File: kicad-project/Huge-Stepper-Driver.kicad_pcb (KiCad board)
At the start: 2 copper layers, 99.1 x 61 mm, 103 parts, among them J1 Screw_Terminal_01x02, J13 Conn_01x04_Male, J14 Conn_01x04_Male, J2 USB_C_Receptacle_USB2.0, J21 Motor 1, J3 Conn_02x04_Odd_Even, J4 Conn_01x02_Female, J5 Conn_01x02_Female, J6 Conn_01x02_Female, J7 Conn_01x04_Male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

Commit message: fix unipolar e qualche rotta
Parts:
- moved R34 1.45 mm to (110.1, 123.6)
- moved R35 1.45 mm to (110.1, 127.4)
- moved R36 1.45 mm to (110.1, 131.1)
- moved R37 1.45 mm to (110.1, 134.9)
- moved R38 1.45 mm to (110.1, 121.8)
- moved R39 1.45 mm to (110.1, 125.5)
- moved R40 1.45 mm to (110.1, 129.3)
- moved R41 1.45 mm to (110.1, 133.0)
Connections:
- D10 pad 1: +12V -> +5V
- D8 pad 1: +12V -> +5V
- D9 pad 1: +12V -> +5V
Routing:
- net GND: track 0.00 -> 27.2 mm, vias 0 -> 6
- net +5V: track 0.00 -> 18.6 mm
- net /Unipolar Driver /M1_OUT1: track 0.00 -> 13.8 mm, vias 0 -> 2
- net /Unipolar Driver /M1_OUT2: track 0.00 -> 12.6 mm, vias 0 -> 2
- net /Unipolar Driver /M1_OUT3: track 0.00 -> 12.3 mm, vias 0 -> 2
- net /Unipolar Driver /M1_OUT4: track 0.00 -> 11.8 mm
- net Net-(Q5-Pad1): track 0.00 -> 6.63 mm
- net Net-(Q8-Pad1): track 0.00 -> 6.60 mm
- net Net-(Q6-Pad1): track 0.00 -> 6.59 mm
- net Net-(Q7-Pad1): track 0.00 -> 6.56 mm

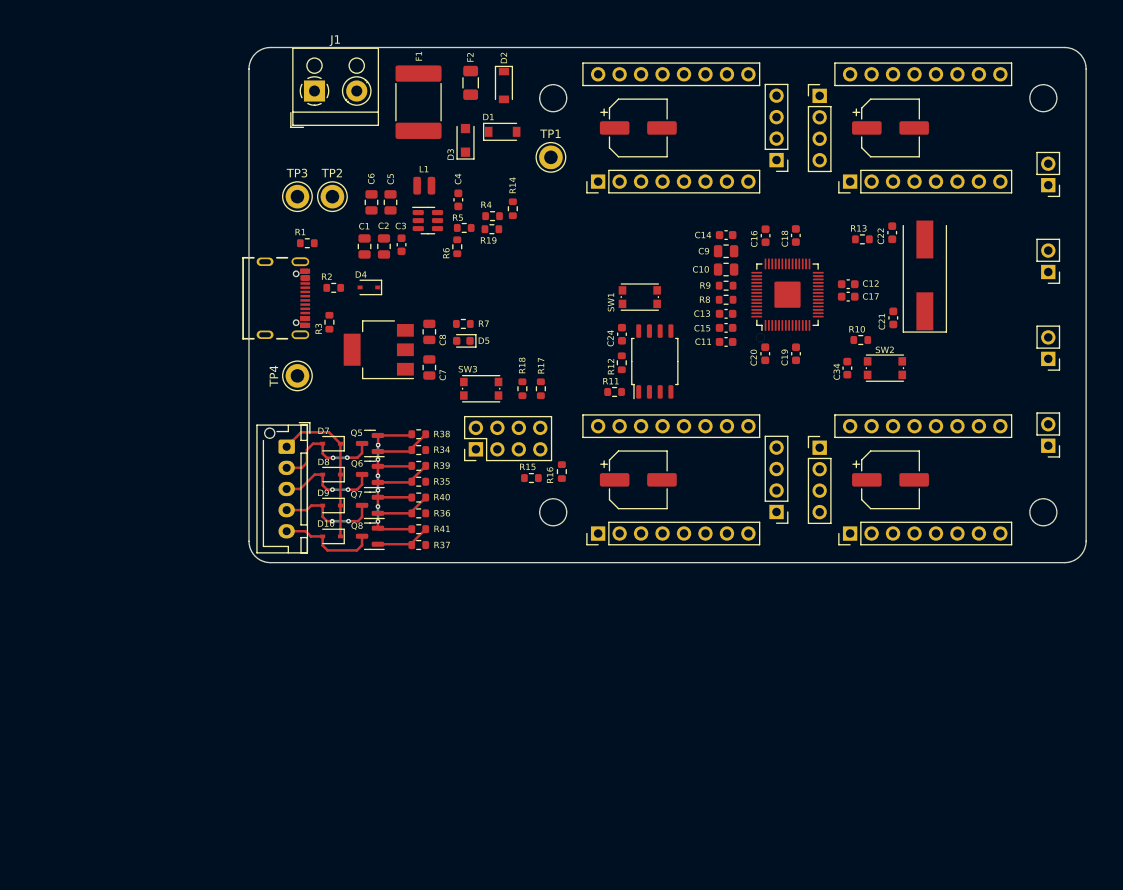
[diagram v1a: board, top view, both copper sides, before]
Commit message: hw: HSD v1.0 w/out peripherals
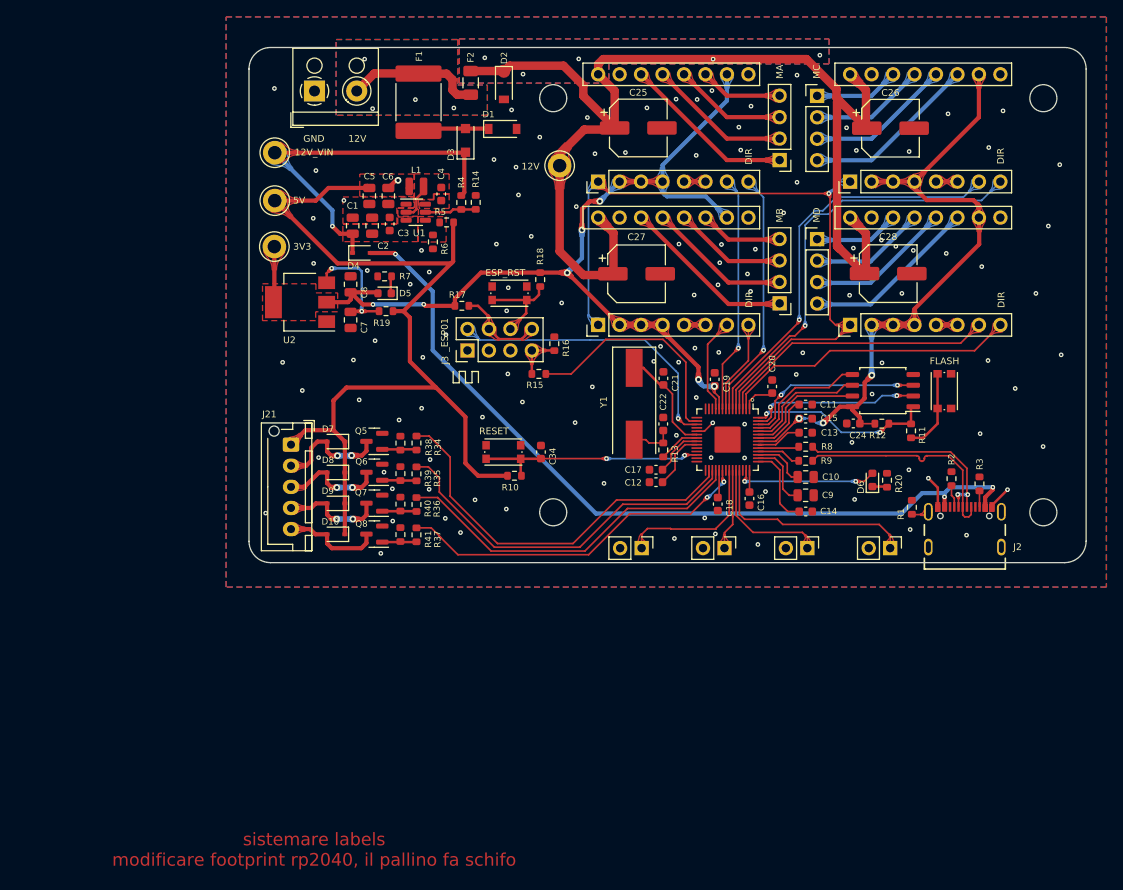
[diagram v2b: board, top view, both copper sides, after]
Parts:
- added D6: PWR_LED, LED_SMD:LED_0603_1608Metric, F.Cu at (163.8, 127.2)
- added R20: 510, Resistor_SMD:R_0603_1608Metric, F.Cu at (165.5, 127.2)
- moved J2 87.9 mm to (174.7, 135.1), turned to 0 degrees
- moved R3 79.3 mm to (176.4, 127.6), turned to 90 degrees
- moved R1 78.1 mm to (168.4, 130.4), turned to 90 degrees
- moved R2 76.5 mm to (173.1, 127.0), turned to 90 degrees
- moved J4 64.5 mm to (136.5, 135.2), turned to -90 degrees
- moved J5 50.4 mm to (146.3, 135.2), turned to -90 degrees
- moved SW2 46.2 mm to (120.1, 123.9), turned to 180 degrees
- moved R10 44.0 mm to (121.4, 126.7)
- moved SW1 37.7 mm to (172.3, 116.7), turned to 90 degrees
- moved Y1 37.6 mm to (135.6, 118.2), turned to -90 degrees
- moved C34 37.6 mm to (124.5, 123.9), turned to 90 degrees
- moved J6 36.3 mm to (156.1, 135.2), turned to -90 degrees
- moved R11 35.4 mm to (168.3, 121.4), turned to 90 degrees
- moved C22 35.3 mm to (139.0, 120.5)
- moved R13 34.3 mm to (139.0, 123.6), turned to -90 degrees
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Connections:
- J3 pad 2: /MCU/ESP_TX -> /MCU/MCU_UART0_RX
- R15 pad 1: /MCU/ESP_RX -> /MCU/MCU_UART0_TX
- R6 pad 1: unconnected-(R6-Pad1) -> GND
- R6 pad 2: unconnected-(R6-Pad2) -> /Power Management/SW_FB
- U3 pad 11: /MCU/STEP_A -> /MCU/STEP_B
- U3 pad 12: /MCU/DIR_A -> unconnected-(U3-Pad12)
- U3 pad 13: /MCU/STEP_B -> unconnected-(U3-Pad13)
- U3 pad 14: /MCU/DIR_B -> unconnected-(U3-Pad14)
- U3 pad 15: /MCU/STEP_C -> unconnected-(U3-Pad15)
- U3 pad 16: /MCU/DIR_C -> /MCU/MCU_UART0_TX
- U3 pad 17: /MCU/STEP_D -> /MCU/MCU_UART0_RX
- U3 pad 18: /MCU/DIR_D -> unconnected-(U3-Pad18)
- U3 pad 2: /MCU/ESP_RX -> /MCU/DIR_D
- U3 pad 27: /MCU/ME_W11 -> unconnected-(U3-Pad27)
- U3 pad 28: /MCU/ME_W12 -> unconnected-(U3-Pad28)
- U3 pad 29: /MCU/ME_W21 -> unconnected-(U3-Pad29)
- U3 pad 3: /MCU/ESP_TX -> /MCU/STEP_D
- U3 pad 30: /MCU/ME_W22 -> /MCU/ME_W11
- U3 pad 31: /Bipolar Drivers/LS1 -> /MCU/ME_W12
- U3 pad 32: /Bipolar Drivers/LS2 -> /MCU/ME_W21
- U3 pad 34: /Bipolar Drivers/LS3 -> /MCU/ME_W22
- U3 pad 35: /Bipolar Drivers/LS4 -> unconnected-(U3-Pad35)
- U3 pad 36: unconnected-(U3-Pad36) -> /Bipolar Drivers/LS1
- U3 pad 37: unconnected-(U3-Pad37) -> /Bipolar Drivers/LS2
- U3 pad 38: unconnected-(U3-Pad38) -> /Bipolar Drivers/LS3
- U3 pad 39: unconnected-(U3-Pad39) -> /Bipolar Drivers/LS4
- U3 pad 4: unconnected-(U3-Pad4) -> /MCU/EN_MOTOR
- U3 pad 41: unconnected-(U3-Pad41) -> Net-(D6-Pad2)
- U3 pad 5: unconnected-(U3-Pad5) -> /MCU/DIR_C
- U3 pad 6: unconnected-(U3-Pad6) -> /MCU/STEP_C
- U3 pad 7: unconnected-(U3-Pad7) -> /MCU/DIR_A
- U3 pad 8: unconnected-(U3-Pad8) -> /MCU/DIR_B
- U3 pad 9: /MCU/EN_MOTOR -> /MCU/STEP_A
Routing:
- net +3V3: track 0.00 -> 236.2 mm, vias 0 -> 10
- net +12V: track 0.00 -> 137.4 mm, vias 0 -> 5
- net /Power Management/VBUS: track 0.00 -> 96.2 mm, vias 0 -> 3
- net +5V: track 18.6 -> 113.9 mm, vias 0 -> 1
- net /MCU/EN_MOTOR: track 0.00 -> 85.0 mm, vias 0 -> 1
- net /MCU/DIR_C: track 0.00 -> 50.7 mm, vias 0 -> 1
- net /MCU/STEP_C: track 0.00 -> 48.3 mm, vias 0 -> 1
- net /MCU/ME_W11: track 0.00 -> 46.6 mm
- net /Power Management/SW_VIN: track 0.00 -> 45.1 mm, vias 0 -> 1
- net /MCU/ME_W12: track 0.00 -> 44.3 mm
- net /MCU/ME_W22: track 0.00 -> 43.0 mm, vias 0 -> 2
- net /MCU/ME_W21: track 0.00 -> 42.7 mm
- net /MCU/DIR_D: track 0.00 -> 35.2 mm
- net /MCU/MCU_UART0_RX: track 0.00 -> 34.9 mm, vias 0 -> 1
- net /MCU/STEP_D: track 0.00 -> 33.2 mm
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- added copper zone on B.Cu, net +12V
- added copper zone on F.Cu, net +12V
- added copper zone on F.Cu, net +3V3
- added copper zone on F.Cu, net +5V
- added copper zone on B.Cu, net /Power Management/12V_IN
- added copper zone on F.Cu, net /Power Management/12V_IN
- added copper zone on F.Cu, net /Power Management/SW_BST
- added copper zone on F.Cu, net /Power Management/SW_FB
- added copper zone on F.Cu, net /Power Management/SW_NODE
- added copper zone on F.Cu, net /Power Management/SW_VIN
- added copper zone on B.Cu, net GND
- added copper zone on F.Cu, net GND
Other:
- board text added: "-"
- board text added: "12V"
- board text added: "12V_VIN"
- board text added: "3V3"
- board text added: "5V"
- board text added: "DIR"
- board text added: "ESP_RST"
- board text added: "FLASH"
- board text added: "GND"
- board text added: "LA"
- board text added: "LB"
- board text added: "LC"
- board text added: "LD"
- board text added: "MA"
- board text added: "MB"
- board text added: "MC"
- board text added: "MD"
- board text added: "RESET"
- board text added: "VIN"
- board text added: "_ESP01"
- board text added: "sistemare labels modificare footprint rp2040, il pallino fa schifo"

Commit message: hw: updated HSD v1.0 + add gerber files
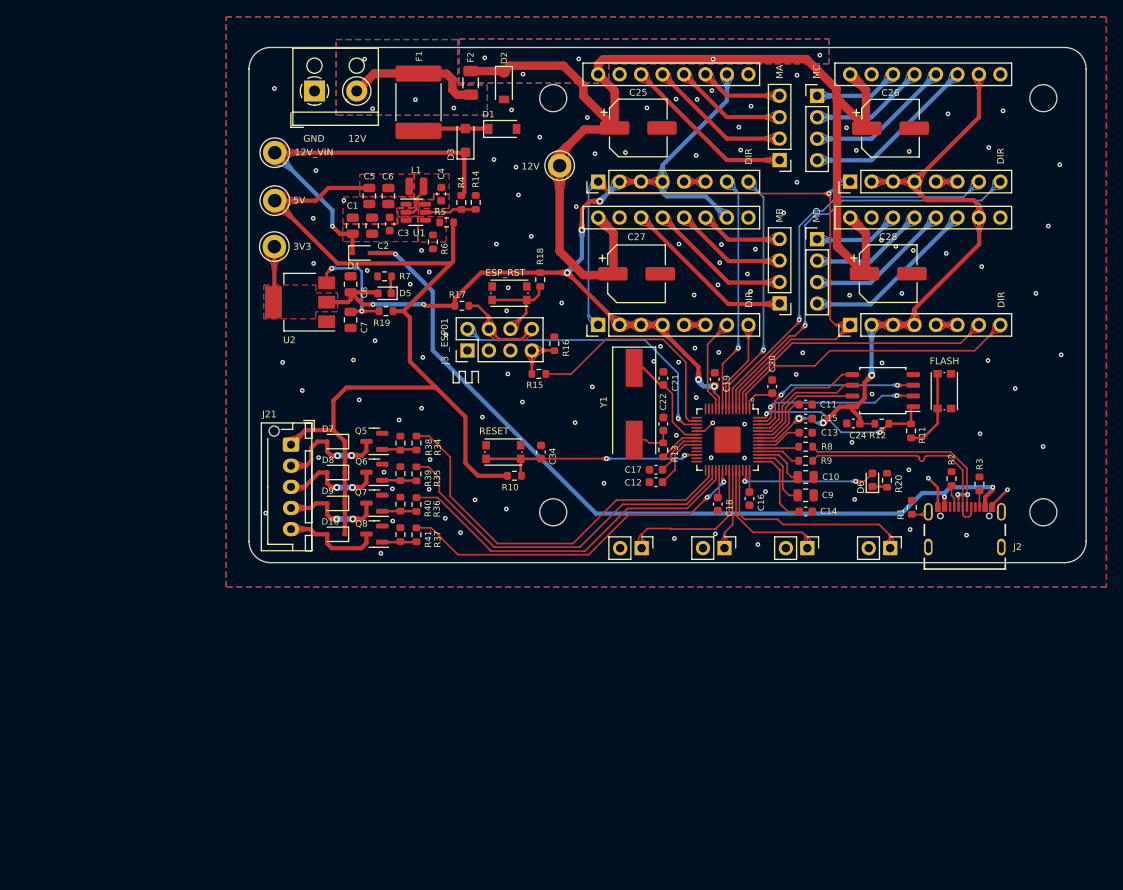
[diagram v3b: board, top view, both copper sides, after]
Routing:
- net +5V: track 113.9 -> 112.4 mm, vias 1 -> 0
- net GND: vias 117 -> 116
- net (no net): vias 1 -> 0
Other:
- board text removed: "100x60mm"
- board text removed: "sistemare labels modificare footprint rp2040, il pallino fa schifo"
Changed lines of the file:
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@@
       (outputformat 1)
       (mirror false)
-      (drillshape 1)
+      (drillshape 0)
       (scaleselection 1)
-      (outputdirectory "")
+      (outputdirectory "/Users/macbookpro/Desktop/HSD-RP2040-5-stepper-motor-driver/kicad-project/gerber")
     )
   )
@@
     (fp_line (start 3.6775 2.56) (end -3.6775 2.56) (layer "F.Fab") (width 0.1))
     (fp_line (start -3.6775 2.56) (end -3.6775 -2.56) (layer "F.Fab") (width 0.1))
-    (pad "1" smd roundrect (at -3.3875 0 90) (size 1.925 5.45) (layers "F.Cu" "F.Paste" "F.Mask") (roundrect_rratio 0.12987)
+    (pad "1" smd roundrect (at -3.3875 0 90) (size 1.925 5.45) (layers "F.Cu" "F.Paste" "F.Mask") (roundrect_rratio 0.1298701299)
       (net 12 "/Power Management/12V_Post_PPTC") (pintype "passive"))
-    (pad "2" smd roundrect (at 3.3875 0 90) (size 1.925 5.45) (layers "F.Cu" "F.Paste" "F.Mask") (roundrect_rratio 0.12987)
+    (pad "2" smd roundrect (at 3.3875 0 90) (size 1.925 5.45) (layers "F.Cu" "F.Paste" "F.Mask") (roundrect_rratio 0.1298701299)
       (net 19 "/Power Management/12V_IN") (pintype "passive"))
     (model "${KICAD6_3DMODEL_DIR}/Fuse.3dshapes/Fuse_2920_7451Metric.wrl"
@@
     (fp_line (start 0 -1.35) (end 0.625 -2.35) (layer "F.Fab") (width 0.1))
     (pad "" np_thru_hole circle (at -1.6 2 270) (size 1.2 1.2) (drill 1.2) (layers *.Cu *.Mask))
-    (pad "1" thru_hole roundrect (at 0 0 270) (size 1.7 1.95) (drill 0.95) (layers *.Cu *.Mask) (roundrect_rratio 0.147059)
+    (pad "1" thru_hole roundrect (at 0 0 270) (size 1.7 1.95) (drill 0.95) (layers *.Cu *.Mask) (roundrect_rratio 0.1470588235)
       (net 5 "+5V") (pinfunction "Pin_1") (pintype "passive"))
     (pad "2" thru_hole oval (at 2.5 0 270) (size 1.7 1.95) (drill 0.95) (layers *.Cu *.Mask)
@@
   (gr_circle (center 126 131) (end 129 131) (layer "Margin") (width 0.15) (fill none))
   (gr_circle (center 184 131) (end 187 131) (layer "Margin") (width 0.15) (fill none))
-  (gr_text "sistemare labels\nmodificare footprint rp2040, il pallino fa schifo" (at 97.71 170.92) (layer "F.Cu")
-    (effects (font (size 1.5 1.5) (thickness 0.3)))
-  )
   (gr_text "3V3" (at 96.35 99.56) (layer "B.SilkS")
     (effects (font (size 0.8 0.8) (thickness 0.15)) (justify mirror))
@@
     (effects (font (size 0.8 0.8) (thickness 0.15)))
   )
-  (gr_text "100x60mm\n" (at 93.525 74.4) (layer "Edge.Cuts")
-    (effects (font (size 1 1) (thickness 0.15)))
-  )
   (gr_text "58x49mm\n" (at 242.75 54.1) (layer "F.Fab")
     (effects (font (size 1 1) (thickness 0.15)))
   )
-  (via (at 161.52 99.74) (size 0.55) (drill 0.25) (layers "F.Cu" "B.Cu") (free) (net 0))
   (segment (start 102.13 98.1814) (end 102.2712 98.0402) (width 0.5) (layer "F.Cu") (net 1))
   (segment (start 93.05 88.45) (end 115.5658 88.45) (width 0.5) (layer "F.Cu") (net 1))
@@
   (via (at 148.64 124.57) (size 0.55) (drill 0.25) (layers "F.Cu" "B.Cu") (free) (net 2))
   (via (at 142.93 117.42) (size 0.55) (drill 0.25) (layers "F.Cu" "B.Cu") (free) (net 2))
-  (via (at 143.93 131.67) (size 0.55) (drill 0.25) (layers "F.Cu" "B.Cu") (free) (net 2))
   (via (at 91.97 131.1) (size 0.55) (drill 0.25) (layers "F.Cu" "B.Cu") (free) (net 2))
   (via (at 137.09 83.15) (size 0.55) (drill 0.25) (layers "F.Cu" "B.Cu") (free) (net 2))
@@
   (segment (start 101.3388 133.6054) (end 101.3388 129.9478) (width 0.5) (layer "F.Cu") (net 5))
   (segment (start 99.9926 121.2864) (end 101.3388 122.6326) (width 0.5) (layer "F.Cu") (net 5))
+  (segment (start 93.05 94.12) (end 97.9 94.12) (width 0.5) (layer "F.Cu") (net 5))
   (segment (start 100.48 101.55) (end 113.92 101.55) (width 0.5) (layer "F.Cu") (net 5))
-  (segment (start 97.9 94.12) (end 99.3998 92.6202) (width 0.5) (layer "F.Cu") (net 5))
+  (segment (start 99.3998 92.6202) (end 104.2374 92.6202) (width 0.5) (layer "F.Cu") (net 5))
   (segment (start 117.1 126.68) (end 120.59 126.68) (width 0.5) (layer "F.Cu") (net 5))
-  (segment (start 107.6374 91.7202) (end 107.3874 91.7202) (width 0.5) (layer "F.Cu") (net 5))
   (segment (start 115.61 119.72) (end 115.61 125.19) (width 0.5) (layer "F.Cu") (net 5))
-  (segment (start 99.3998 92.6202) (end 104.2374 92.6202) (width 0.5) (layer "F.Cu") (net 5))
   (segment (start 112.13 116.24) (end 115.61 119.72) (width 0.5) (layer "F.Cu") (net 5))
   (segment (start 93.05 94.12) (end 100.48 101.55) (width 0.5) (layer "F.Cu") (net 5))
@@
   (segment (start 96.6782 121.2864) (end 99.9926 121.2864) (width 0.5) (layer "F.Cu") (net 5))
   (segment (start 112.13 116.24) (end 109.04 113.15) (width 0.5) (layer "F.Cu") (net 5))
-  (segment (start 93.05 94.12) (end 97.9 94.12) (width 0.5) (layer "F.Cu") (net 5))
   (segment (start 108.27 107.2) (end 114.1574 101.3126) (width 0.5) (layer "F.Cu") (net 5))
   (segment (start 101.3388 129.9478) (end 101.3388 126.2902) (width 0.5) (layer "F.Cu") (net 5))
@@
   (segment (start 113.92 101.55) (end 114.1574 101.3126) (width 0.5) (layer "F.Cu") (net 5))
   (segment (start 94.9726 122.992) (end 96.6782 121.2864) (width 0.5) (layer "F.Cu") (net 5))
-  (segment (start 107.3874 91.7202) (end 106.4874 92.6202) (width 0.5) (layer "F.Cu") (net 5))
   (segment (start 99.9926 117.7774) (end 101.53 116.24) (width 0.5) (layer "F.Cu") (net 5))
   (segment (start 101.53 116.24) (end 112.13 116.24) (width 0.5) (layer "F.Cu") (net 5))
   (segment (start 108.7774 92.6202) (end 108.9574 92.4402) (width 0.5) (layer "F.Cu") (net 5))
-  (via (at 107.6374 91.7202) (size 0.8) (drill 0.4) (layers "F.Cu" "B.Cu") (net 5))
+  (segment (start 97.9 94.12) (end 99.3998 92.6202) (width 0.5) (layer "F.Cu") (net 5))
   (segment (start 155.065055 121.582545) (end 154.9578 121.6898) (width 0.2) (layer "F.Cu") (net 6))
   (segment (start 152.331424 122.6034) (end 150.2675 122.6034) (width 0.2) (layer "F.Cu") (net 6))
@@
     )
   )
-  (zone (net 6) (net_name "+3V3") (layer "F.Cu") (hatch edge 0.508)
+  (zone (net 6) (net_name "+3V3") (layer "F.Cu") (name "3V3") (hatch edge 0.508)
+    (priority 1)
     (connect_pads (clearance 0.508))
     (min_thickness 0.254) (filled_areas_thickness no)
@@
         (xy 100.49 107.27)
         (xy 97.89 107.27)
-        (xy 97.89 108.32)
-        (xy 91.6 108.32)
-        (xy 91.6 103.96)
-        (xy 97.92 103.96)
+        (xy 97.89 108.1)
+        (xy 91.74 108.1)
+        (xy 91.74 104.11)
+        (xy 97.92 104.11)
       )
     )

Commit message: hw: update HSD v1.0
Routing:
- net +3V3: track 236.2 -> 264.2 mm
- net +1V1: track 21.2 -> 33.4 mm, vias 0 -> 3
- net GND: track 9.17 -> 9.43 mm, vias 116 -> 111
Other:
- board text added: "BOTTOM"
- board text added: "TOP"

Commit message: nuovi gerber e credits
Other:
- board text added: "Designed by Lisa Santarossa and Damiano Pedoni"
- board text added: "JLCJLCJLCJLC"
- board text added: "at University of Trento"
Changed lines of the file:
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@@
     (pad_to_mask_clearance 0)
     (pcbplotparams
-      (layerselection 0x00010fc_ffffffff)
+      (layerselection 0x0000008_7ffffffe)
       (disableapertmacros false)
       (usegerberextensions false)
@@
       (creategerberjobfile true)
       (svguseinch false)
-      (svgprecision 6)
+      (svgprecision 3)
       (excludeedgelayer true)
       (plotframeref false)
@@
       (sketchpadsonfab false)
       (subtractmaskfromsilk false)
-      (outputformat 1)
+      (outputformat 5)
       (mirror false)
       (drillshape 0)
       (scaleselection 1)
-      (outputdirectory "/Users/macbookpro/Desktop/HSD-RP2040-5-stepper-motor-driver/kicad-project/gerber")
+      (outputdirectory "new gerbers/")
     )
   )
@@
     (effects (font (size 0.8 0.8) (thickness 0.15)) (justify mirror))
   )
+  (gr_text "Designed by Lisa Santarossa and Damiano Pedoni" (at 139.4206 122.0216) (layer "B.SilkS")
+    (effects (font (size 0.8 0.8) (thickness 0.15)) (justify mirror))
+  )
   (gr_text "VIN" (at 96.27 88.36) (layer "B.SilkS")
     (effects (font (size 0.8 0.8) (thickness 0.15)) (justify mirror))
@@
     (effects (font (size 0.8 0.8) (thickness 0.15)) (justify mirror))
   )
+  (gr_text "at University of Trento" (at 139.573 123.8504) (layer "B.SilkS")
+    (effects (font (size 0.75 0.75) (thickness 0.15)) (justify mirror))
+  )
   (gr_text "LB" (at 146.28 132.75) (layer "B.SilkS")
     (effects (font (size 0.8 0.8) (thickness 0.15)) (justify mirror))
@@
     (effects (font (size 0.8 0.8) (thickness 0.15)) (justify mirror))
   )
+  (gr_text "JLCJLCJLCJLC" (at 187.5028 121.793 90) (layer "B.SilkS")
+    (effects (font (size 1 1) (thickness 0.15)) (justify mirror))
+  )
   (gr_text "12V" (at 102.82 86.79) (layer "F.SilkS")
